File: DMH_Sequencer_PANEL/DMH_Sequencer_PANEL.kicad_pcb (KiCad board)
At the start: 2 copper layers, 300 x 200 mm, 89 parts, among them J0 Panel_GND_Solder_Wire_Pad

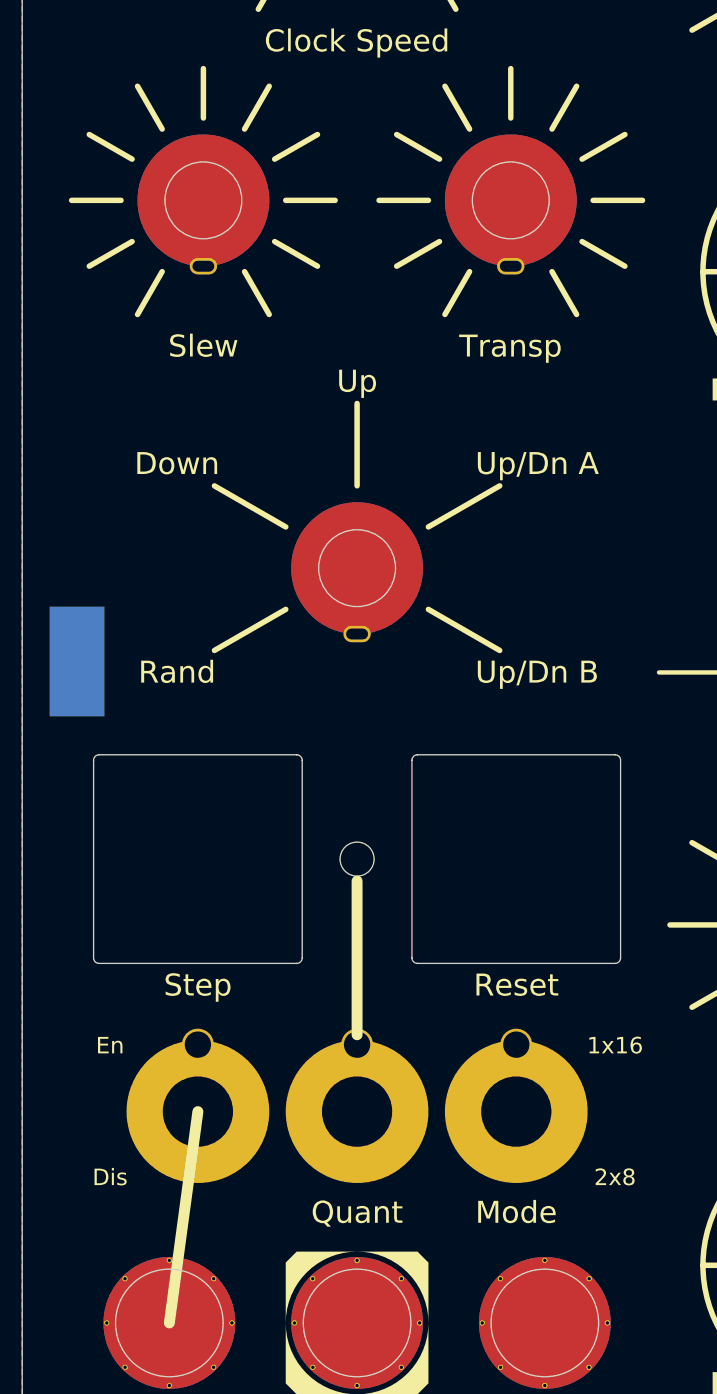
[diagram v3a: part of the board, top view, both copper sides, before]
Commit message: Added clock PPQN selector
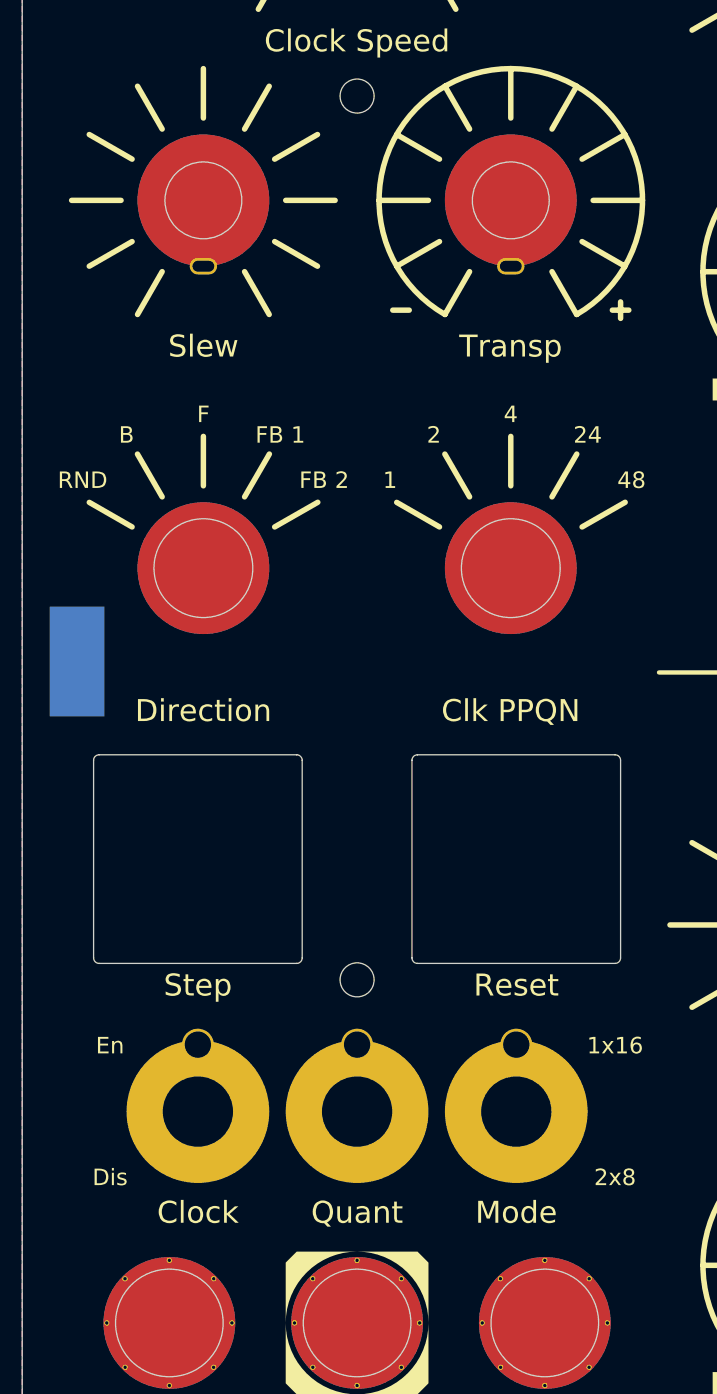
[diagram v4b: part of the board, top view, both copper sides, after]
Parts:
- added H98: LED Clock, SynthStuff:MountingHole_LED_3mm_R, F.Cu at (80.5, 78.5)
- added H99: Clk PPQN, SynthStuff:Selector_Cutout_SRBV151102, F.Cu at (94.5, 121.5)
- H75: footprint SynthStuff:Pot_Cutout_Tiny -> SynthStuff:Pot_Cutout_Tiny_attv_RD901F
- H79: footprint SynthStuff:Selector_Cutout_5pos -> SynthStuff:Selector_Cutout_SRBV151102
- moved H79 14.0 mm to (66.5, 121.5)
- moved H85 11.0 mm to (80.5, 159.0)

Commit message: jack placemente ongoig
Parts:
- added H100: Gate 1, SynthStuff:Jack_6.35mm_Cutout_Output_v6, F.Cu at (131.5, 118.0)
- added H101: Gate 2, SynthStuff:Jack_6.35mm_Cutout_Output_v6, F.Cu at (161.5, 118.0)
- added H102: Gate 3, SynthStuff:Jack_6.35mm_Cutout_Output_v6, F.Cu at (191.5, 118.0)
- added H103: Gate 4, SynthStuff:Jack_6.35mm_Cutout_Output_v6, F.Cu at (221.5, 118.0)
- added H104: Gate 5, SynthStuff:Jack_6.35mm_Cutout_Output_v6, F.Cu at (251.5, 118.0)
- added H105: Gate 6, SynthStuff:Jack_6.35mm_Cutout_Output_v6, F.Cu at (281.5, 118.0)
- added H106: Gate 7, SynthStuff:Jack_6.35mm_Cutout_Output_v6, F.Cu at (311.5, 118.0)
- added H107: Gate 8, SynthStuff:Jack_6.35mm_Cutout_Output_v6, F.Cu at (341.5, 118.0)
- added H108: Gate 9, SynthStuff:Jack_6.35mm_Cutout_Output_v6, F.Cu at (399.0, 74.5)
- added H109: Gate 10, SynthStuff:Jack_6.35mm_Cutout_Output_v6, F.Cu at (406.7, 99.8)
- added H110: Gate 11, SynthStuff:Jack_6.35mm_Cutout_Output_v6, F.Cu at (406.7, 116.9)
- added H111: Gate 12, SynthStuff:Jack_6.35mm_Cutout_Output_v6, F.Cu at (406.7, 134.0)
- added H112: Gate 13, SynthStuff:Jack_6.35mm_Cutout_Output_v6, F.Cu at (423.8, 82.7)
- added H113: Gate 14, SynthStuff:Jack_6.35mm_Cutout_Output_v6, F.Cu at (423.8, 99.8)
- added H114: Gate 15, SynthStuff:Jack_6.35mm_Cutout_Output_v6, F.Cu at (423.8, 116.9)
- added H115: Gate 16, SynthStuff:Jack_6.35mm_Cutout_Output_v6, F.Cu at (423.8, 134.0)
- moved H25 7.50 mm to (116.5, 118.0)
- moved H26 7.50 mm to (146.5, 118.0)
- moved H27 7.50 mm to (176.5, 118.0)
- moved H28 7.50 mm to (206.5, 118.0)
- moved H29 7.50 mm to (236.5, 118.0)
- moved H30 7.50 mm to (266.5, 118.0)
- moved H31 7.50 mm to (296.5, 118.0)
- moved H32 7.50 mm to (326.5, 118.0)
- moved H57 7.50 mm to (116.5, 208.5)
- moved H58 7.50 mm to (146.5, 208.5)
- moved H59 7.50 mm to (176.5, 208.5)
- moved H60 7.50 mm to (206.5, 208.5)
- moved H61 7.50 mm to (236.5, 208.5)
- moved H62 7.50 mm to (266.5, 208.5)
- moved H63 7.50 mm to (296.5, 208.5)
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
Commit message: Positioning 1 done
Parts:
- moved H108 299.2 mm to (131.5, 208.5)
- moved H109 268.3 mm to (161.5, 208.5)
- moved H110 233.9 mm to (191.5, 208.5)
- moved H112 213.4 mm to (251.5, 208.5)
- moved H111 199.7 mm to (221.5, 208.5)
- moved H113 179.1 mm to (281.5, 208.5)
- moved H114 145.0 mm to (311.5, 208.5)
- moved H115 111.1 mm to (341.5, 208.5)

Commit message: Redistributed glide switches and gate outs
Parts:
- H100: value Gate 1 -> 1
- H101: value Gate 2 -> 2
- H102: value Gate 3 -> 3
- H103: value Gate 4 -> 4
- H104: value Gate 5 -> 5
- H105: value Gate 6 -> 6
- H106: value Gate 7 -> 7
- H107: value Gate 8 -> 8
- H108: value Gate 9 -> 9
- H109: value Gate 10 -> 10
- H110: value Gate 11 -> 11
- H111: value Gate 12 -> 12
- H112: value Gate 13 -> 13
- H113: value Gate 14 -> 14
- H114: value Gate 15 -> 15
- H115: value Gate 16 -> 16
- H25: value Slew 1 -> 1
- H26: value Slew 2 -> 2
- H27: value Slew 3 -> 3
- H28: value Slew 4 -> 4
- H29: value Slew 5 -> 5
- H30: value Slew 6 -> 6
- H31: value Slew 7 -> 7
- H32: value Slew 8 -> 8
- H57: value Slew 9 -> 9
- H58: value Slew 10 -> 10
- H59: value Slew 11 -> 11
- H60: value Slew 12 -> 12
- H61: value Slew 13 -> 13
- H62: value Slew 14 -> 14
- H63: value Slew 15 -> 15
- H64: value Slew 16 -> 16
- H77: value Slew -> Glide
- moved H32 133.7 mm to (214.0, 190.2)
- moved H100 121.5 mm to (229.0, 190.5)
- moved H31 120.6 mm to (200.0, 190.2)
- moved H64 112.5 mm to (214.0, 208.8)
- moved H101 110.6 mm to (245.0, 190.5)
- moved H30 108.2 mm to (186.0, 190.2)
- moved H102 100.4 mm to (261.0, 190.5)
- moved H108 97.5 mm to (229.0, 209.0)
- moved H29 96.9 mm to (172.0, 190.2)
- moved H63 96.5 mm to (200.0, 208.8)
- moved H103 91.3 mm to (277.0, 190.5)
- moved H28 87.0 mm to (158.0, 190.2)
- moved H104 83.5 mm to (293.0, 190.5)
- moved H109 83.5 mm to (245.0, 209.0)
- moved H62 80.5 mm to (186.0, 208.8)
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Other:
- board text added: "Glide"
- board text added: "Individual Gate Out"

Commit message: Update DMH_Sequencer_PANEL.kicad_pcb
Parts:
- H77: value Glide -> Slew
- moved H73 0.50 mm to (80.0, 55.0)
- moved H75 0.50 mm to (94.0, 88.0)
- moved H77 0.50 mm to (66.0, 88.0)
- moved H79 0.50 mm to (66.0, 121.5)
- moved H80 0.50 mm to (94.5, 171.0)
- moved H81 0.50 mm to (65.5, 171.0)
- moved H82 0.50 mm to (80.0, 171.0)
- moved H83 0.50 mm to (65.5, 148.0)
- moved H84 0.50 mm to (94.5, 148.0)
- moved H85 0.50 mm to (80.0, 159.0)
- moved H86 0.50 mm to (62.9, 208.8)
- moved H87 0.50 mm to (80.0, 208.8)
- moved H88 0.50 mm to (97.1, 208.8)
- moved H90 0.50 mm to (62.9, 190.2)
- moved H91 0.50 mm to (97.1, 190.2)
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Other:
- board text added: "Burst"
- board text added: "Cont"
- board text added: "Slew / Manual Gate"
- board text added: "off"
- board text removed: "Dis"
- board text removed: "En"
- board text removed: "Glide"
